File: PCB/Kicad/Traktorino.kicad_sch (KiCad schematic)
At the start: 4 parts

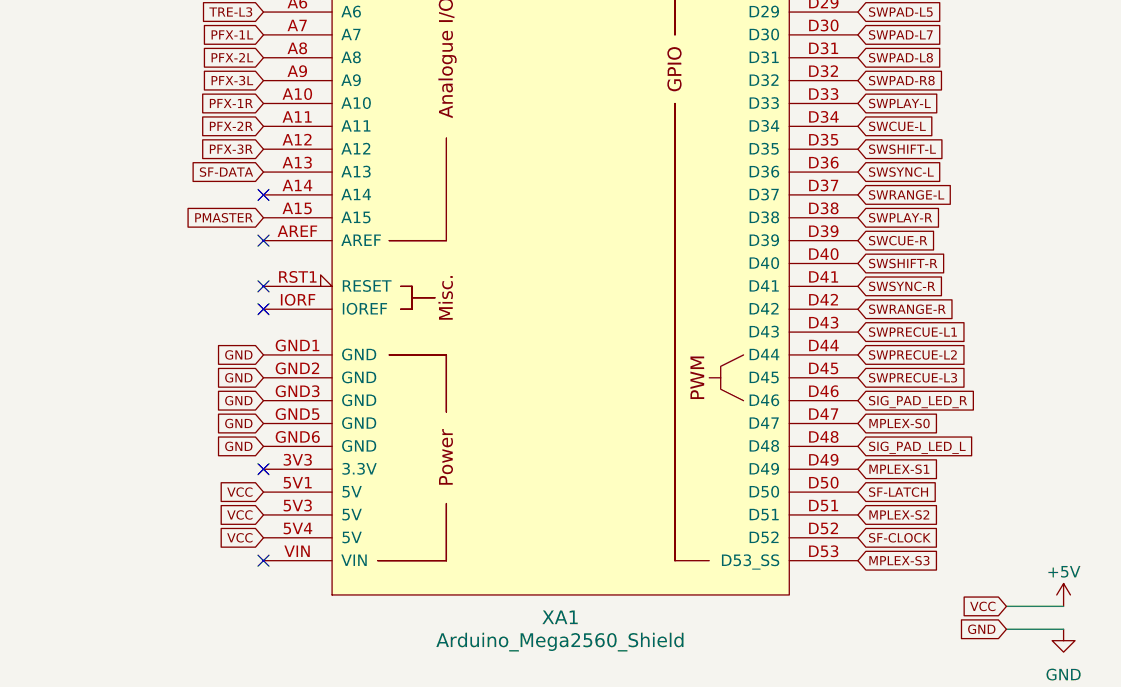
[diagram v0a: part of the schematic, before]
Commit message: fixing 3dmodels
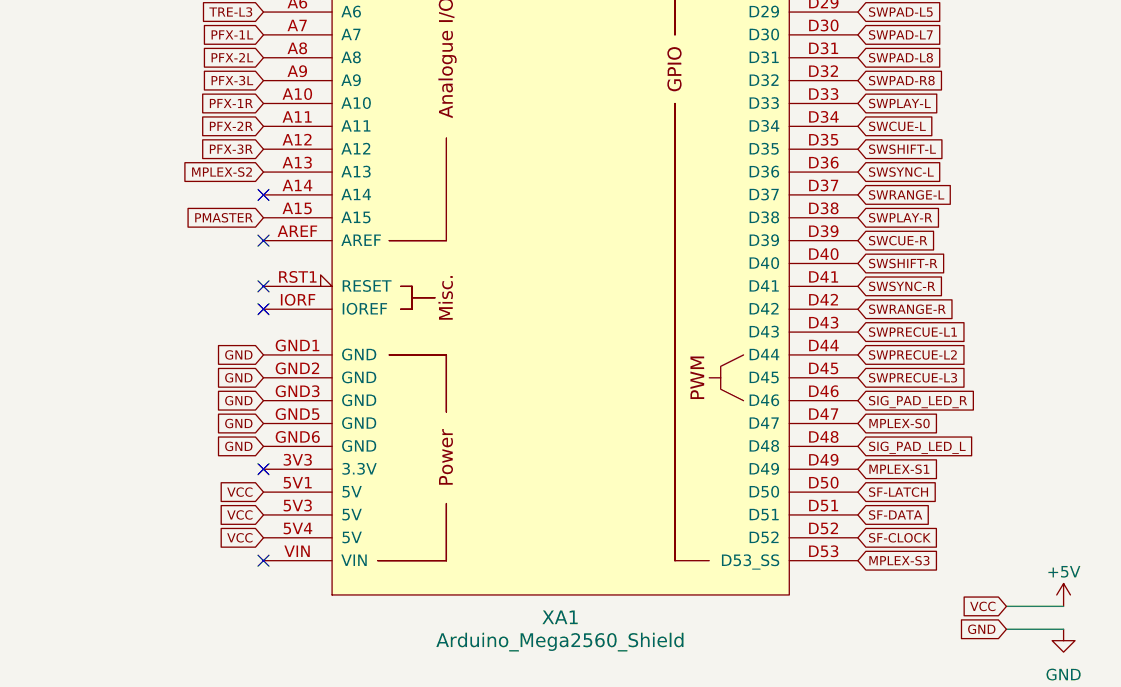
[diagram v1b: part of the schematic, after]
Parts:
- IC-POTS-1: footprint Package_SO:SOIC-24W_7.5x15.4mm_P1.27mm -> Library:SOIC-24W_7.5x15.4mm_P1.27mm
- XA1: footprint Arduino:Arduino_Mega2560_Shield -> Library:Arduino_Mega2560_Shield
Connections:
- net MPLEX-S2: now also XA1.A13; no longer XA1.D51
- net SF-DATA: now also XA1.D51; no longer XA1.A13

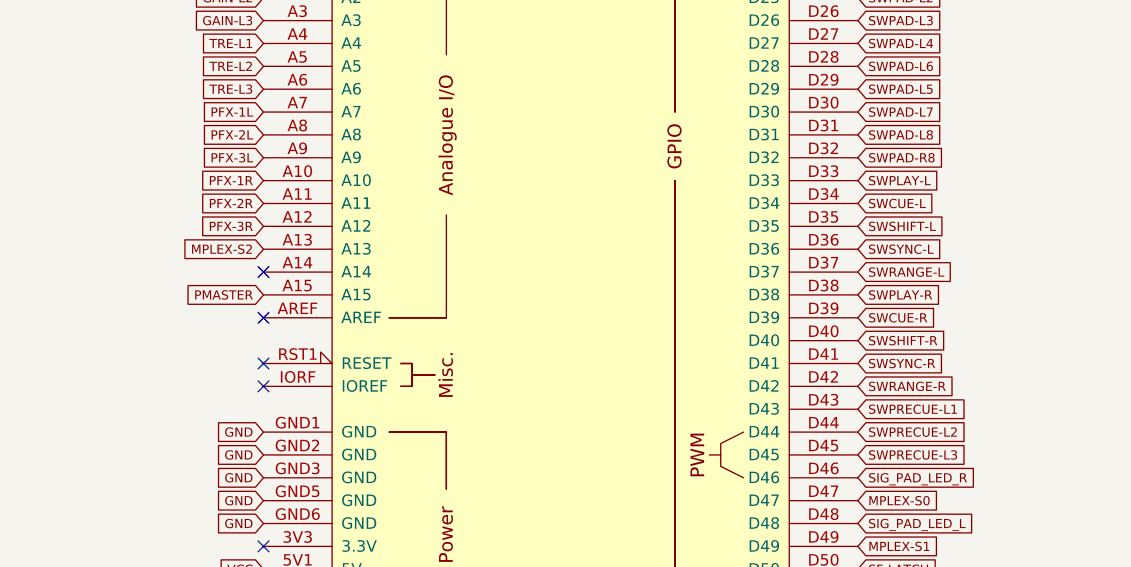
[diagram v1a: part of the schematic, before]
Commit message: change few pins  and programming
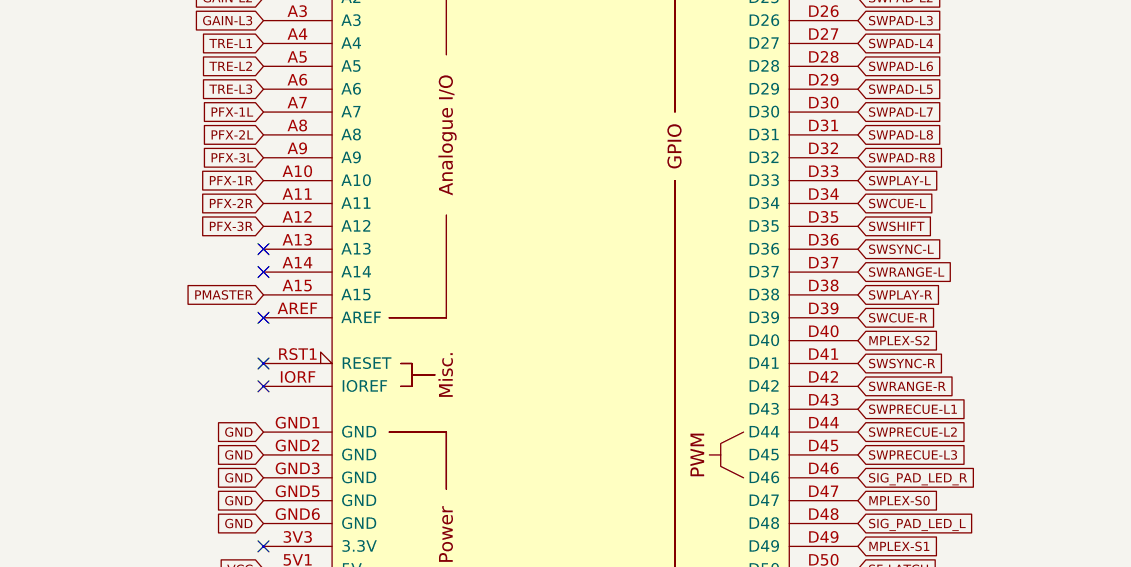
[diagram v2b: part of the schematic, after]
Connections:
- net SWSHIFT-R is gone; now on net MPLEX-S2: XA1.D40
- net MPLEX-S2: no longer XA1.A13
- net SWSHIFT-L renamed SWSHIFT
- no-connect marks 8 -> 9
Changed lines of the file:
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@@
   (no_connect (at 127.635 64.77))
   (no_connect (at 127.635 67.31))
+  (no_connect (at 127.635 105.41))
   (no_connect (at 127.635 107.95))
   (no_connect (at 127.635 113.03))
@@
     )
   )
-  (global_label "MPLEX-S2" (shape input) (at 127.635 105.41 180)
-    (effects (font (size 1.016 1.016)) (justify right))
-    (property "Intersheet References" "${INTERSHEET_REFS}" (id 0) (at 117.625 105.4735 0)
-      (effects (font (size 1.016 1.016)) (justify right) hide)
-    )
-  )
   (global_label "PMASTER" (shape input) (at 127.635 110.49 180)
     (effects (font (size 1.016 1.016)) (justify right))
@@
     )
   )
-  (global_label "SWSHIFT-L" (shape input) (at 193.675 102.87 0)
-    (effects (font (size 1.016 1.016)) (justify left))
-    (property "Intersheet References" "${INTERSHEET_REFS}" (id 0) (at 81.915 36.83 0)
-      (effects (font (size 1.27 1.27)) hide)
+  (global_label "SWSHIFT" (shape input) (at 193.675 102.87 0)
+    (effects (font (size 1.016 1.016)) (justify left))
+    (property "Intersheet References" "${INTERSHEET_REFS}" (id 0) (at 201.8949 102.8065 0)
+      (effects (font (size 1.016 1.016)) (justify left) hide)
     )
   )
@@
     )
   )
-  (global_label "SWSHIFT-R" (shape input) (at 193.675 115.57 0)
-    (effects (font (size 1.016 1.016)) (justify left))
-    (property "Intersheet References" "${INTERSHEET_REFS}" (id 0) (at 47.625 49.53 0)
-      (effects (font (size 1.27 1.27)) hide)
+  (global_label "MPLEX-S2" (shape input) (at 193.675 115.57 0)
+    (effects (font (size 1.016 1.016)) (justify left))
+    (property "Intersheet References" "${INTERSHEET_REFS}" (id 0) (at 203.685 115.5065 0)
+      (effects (font (size 1.016 1.016)) (justify left) hide)
     )
   )
@@
   (sheet (at 31.75 24.13) (size 48.26 38.1)
     (stroke (width 0) (type solid) (color 0 0 0 0))
-    (fill (color 0 0 0 0.0000))
+    (fill (color 72 72 72 1.0000))
     (property "Sheet name" "LedsSheet" (id 0) (at 31.75 23.6215 0)
       (effects (font (size 1.016 1.016)) (justify left bottom))
@@
   (sheet (at 33.02 132.08) (size 46.99 33.02)
     (stroke (width 0.0006) (type solid) (color 0 0 0 0))
-    (fill (color 0 0 0 0.0000))
+    (fill (color 72 72 72 1.0000))
     (property "Sheet name" "PadLedsSheet" (id 0) (at 33.02 131.4443 0)
       (effects (font (size 1.27 1.27)) (justify left bottom))
@@
   (sheet (at 225.425 69.215) (size 45.72 33.02)
     (stroke (width 0) (type solid) (color 0 0 0 0))
-    (fill (color 0 0 0 0.0000))
+    (fill (color 72 72 72 1.0000))
     (property "Sheet name" "PotenciometersSheet" (id 0) (at 225.425 68.7065 0)
       (effects (font (size 1.016 1.016)) (justify left bottom))
@@
   (sheet (at 31.877 77.4446) (size 50.673 36.8554)
     (stroke (width 0) (type solid) (color 0 0 0 0))
-    (fill (color 0 0 0 0.0000))
+    (fill (color 72 72 72 1.0000))
     (property "Sheet name" "ShiftRegistersSheet" (id 0) (at 31.877 76.8091 0)
       (effects (font (size 1.27 1.27)) (justify left bottom))
@@
   (sheet (at 226.695 26.035) (size 40.64 35.56)
     (stroke (width 0) (type solid) (color 0 0 0 0))
-    (fill (color 0 0 0 0.0000))
+    (fill (color 72 72 72 1.0000))
     (property "Sheet name" "SwitchersSheet" (id 0) (at 226.695 25.5265 0)
       (effects (font (size 1.016 1.016)) (justify left bottom))
